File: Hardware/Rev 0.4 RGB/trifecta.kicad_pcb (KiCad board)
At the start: 2 copper layers, 361 x 120.8 mm, 264 parts, among them J1 USB2_C_Receptacle, SW1 SW_Push, SW2 Rotary_Encoder_Switch, SW3 Rotary_Encoder_Switch, SW4 Rotary_Encoder_Switch, U1 ATmega32U4-AU, U2 SRV05-4, Y1 16MHz

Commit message: Changes
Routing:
- net col1: track 99.0 -> 316.3 mm, vias 0 -> 3
- net col2: track 0.00 -> 174.6 mm
- net col3: track 0.00 -> 74.9 mm
- net row1: track 0.45 -> 46.5 mm
- net row0: track 0.26 -> 26.3 mm
- removed copper zone on F.Cu, net GND

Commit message: Update
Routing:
- net col2: track 174.6 -> 235.5 mm, vias 0 -> 2
- net col3: track 74.9 -> 95.1 mm, vias 0 -> 3
- net GND: track 2408.1 -> 2403.4 mm, vias 136 -> 137

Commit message: 03/08-1
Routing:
- net row1: track 46.5 -> 266.6 mm, vias 0 -> 2
- net row0: track 26.3 -> 199.3 mm, vias 0 -> 2
- net row4: track 0.09 -> 148.9 mm, vias 0 -> 4
- net row9: track 0.00 -> 136.2 mm
- net row8: track 0.00 -> 99.6 mm, vias 0 -> 2
- net row6: track 0.61 -> 98.2 mm, vias 0 -> 2
- net row2: track 0.24 -> 88.6 mm, vias 0 -> 2
- net row5: track 0.32 -> 85.9 mm
- net row3: track 2.36 -> 69.7 mm, vias 0 -> 2
- net row7: track 1.46 -> 48.6 mm
- net Net-(LED21-Pad2): track 42.9 -> 50.0 mm
- net +5V: track 1917.1 -> 1920.0 mm, vias 66 -> 67
- net GND: vias 137 -> 136

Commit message: 8/3/2020
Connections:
- U1 pad 10: row6 -> col5
- U1 pad 18: row7 -> col6
- U1 pad 19: row8 -> col4
- U1 pad 29: col6 -> row7
- U1 pad 31: row3 -> row5
- U1 pad 32: col5 -> row6
- U1 pad 37: col4 -> row8
- U1 pad 9: row5 -> row3
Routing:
- net 0col: track 11.0 -> 475.3 mm, vias 0 -> 1
- net col6: track 0.00 -> 355.4 mm, vias 0 -> 2
- net row3: track 69.7 -> 408.9 mm, vias 2 -> 7
- net col5: track 0.00 -> 333.3 mm, vias 0 -> 1
- net row7: track 48.6 -> 377.5 mm
- net row8: track 99.6 -> 412.2 mm, vias 2 -> 5
- net ENC0B: track 0.00 -> 281.1 mm, vias 0 -> 1
- net row9: track 136.2 -> 409.3 mm, vias 0 -> 3
- net ENCB: track 272.8 -> 0.00 mm
- net row2: track 88.6 -> 358.4 mm, vias 2 -> 6
- net row6: track 98.2 -> 354.4 mm, vias 2 -> 4
- net col4: track 0.56 -> 256.4 mm, vias 0 -> 2
- net row5: track 85.9 -> 337.5 mm, vias 0 -> 3
- net ENC2B: track 0.00 -> 224.4 mm, vias 0 -> 2
- net ENC1B: track 0.00 -> 206.8 mm
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
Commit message: Clean up silkscreens, Add ground fill, Generate new gerbers
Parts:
- R1, R6: value 10k -> 10kΩ
- R2, R3: value 5.1k -> 5.1kΩ
- R4, R5: value 22 -> 22Ω
- SW1: value SW_Push -> RESET
- moved SW2 0.22 mm to (323.9, 9.50)
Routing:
- net GND: vias 129 -> 143
- added copper zone on F.Cu, net GND

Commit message: Edit resistor silkscreen, Generate Gerbers
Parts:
- R7: value 510 ohm -> 510Ω
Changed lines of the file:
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@@
     (46 B.CrtYd user)
     (47 F.CrtYd user)
-    (48 B.Fab user)
+    (48 B.Fab user hide)
     (49 F.Fab user hide)
   )
@@
     (tags resistor)
     (attr smd)
-    (fp_text reference R7 (at 0 1.65 270) (layer B.SilkS)
+    (fp_text reference R7 (at 0 1.65 270) (layer B.Fab)
       (effects (font (size 1 1) (thickness 0.15)) (justify mirror))
     )
-    (fp_text value "510 ohm" (at 0 -1.65 270) (layer B.Fab)
+    (fp_text value 510Ω (at 0 1.65104 270) (layer B.SilkS)
       (effects (font (size 1 1) (thickness 0.15)) (justify mirror))
     )

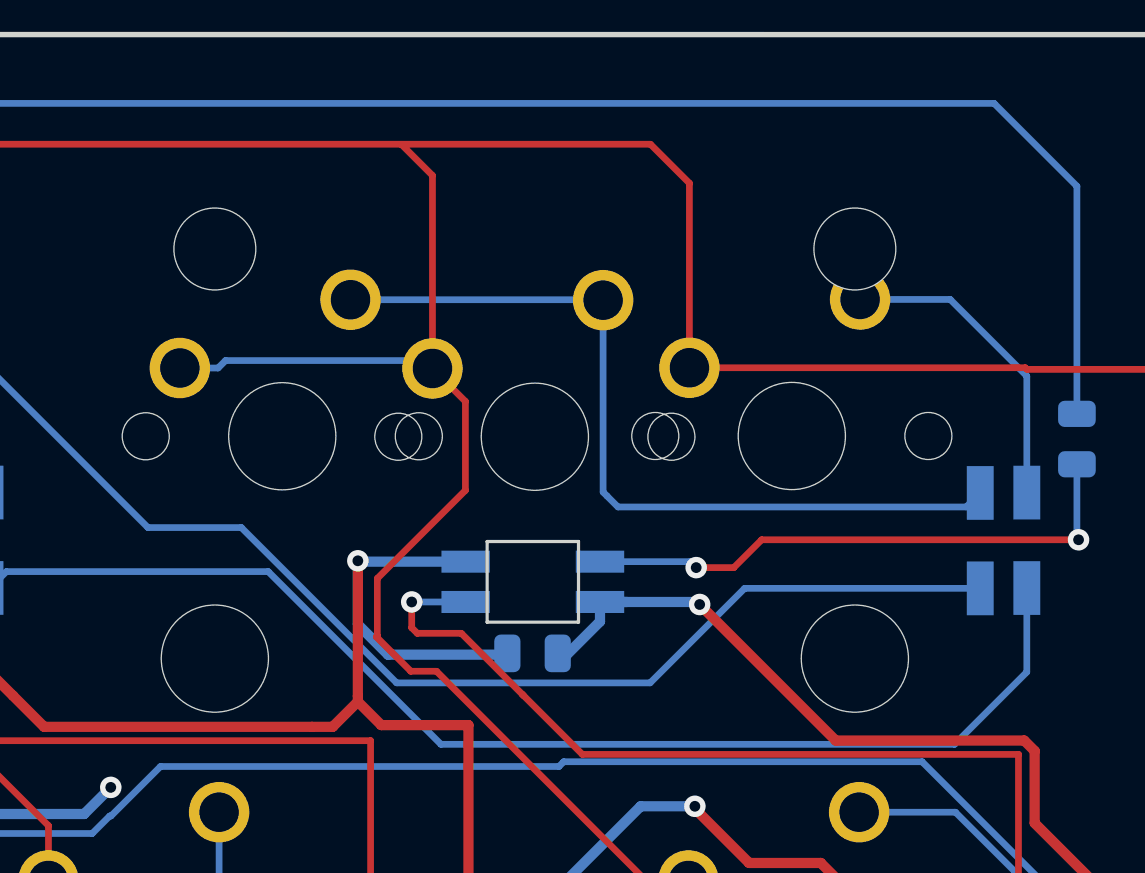
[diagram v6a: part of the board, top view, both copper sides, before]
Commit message: Flip backspace stab regenerate gerbers
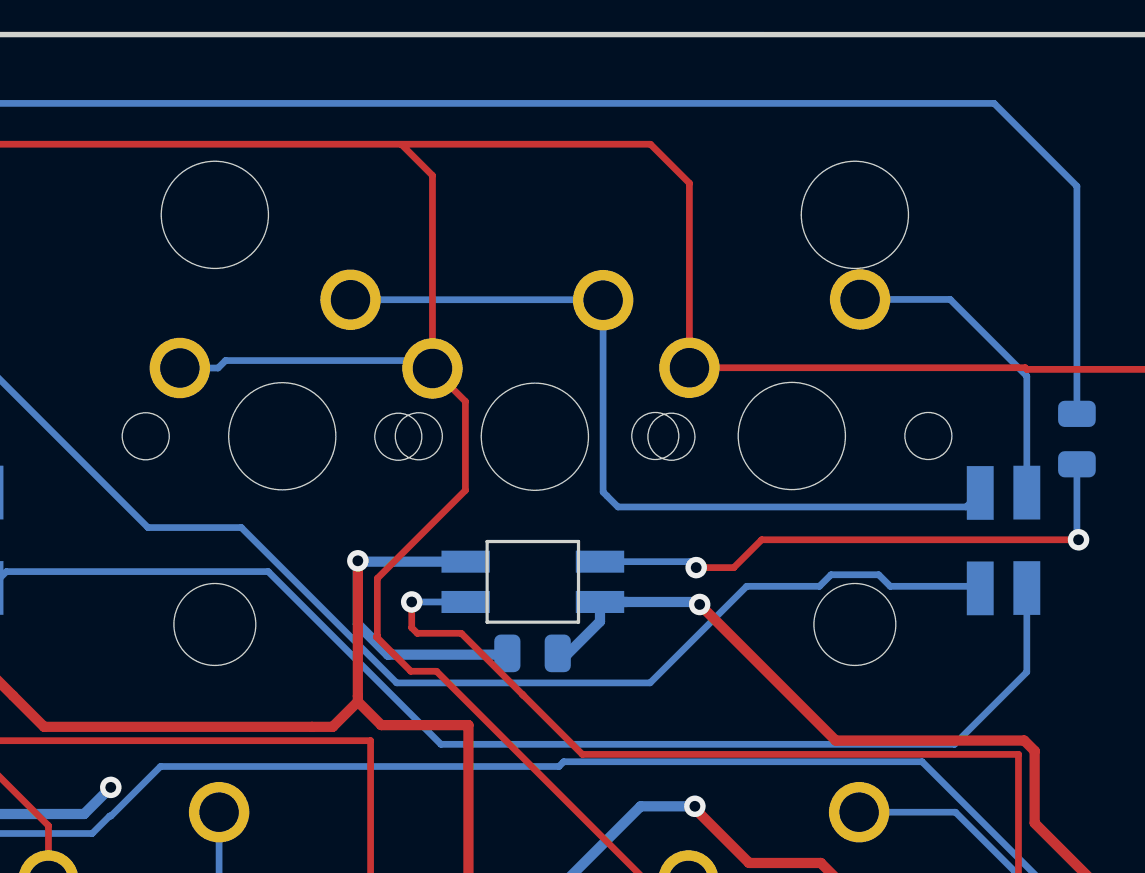
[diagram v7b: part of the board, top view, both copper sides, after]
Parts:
- K_15: footprint MX_Only:MXOnly-2U-NoLED -> MX_Only:MXOnly-2U-ReversedStabilizers-NoLED
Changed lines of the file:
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@@
     (thickness 1.6)
     (drawings 941)
-    (tracks 4299)
+    (tracks 4304)
     (zones 0)
     (modules 264)
@@
     (add_net VBUS)
   )
+  (module MX_Only:MXOnly-2U-ReversedStabilizers-NoLED (layer F.Cu)
+    (at 285.78125 9.434746)
+    (fp_text reference K_15 (at 0 3.175) (layer Dwgs.User)
+      (effects (font (size 1 1) (thickness 0.15)))
+    )
+    (fp_text value KEYSW (at 0 -7.9375) (layer Dwgs.User)
+      (effects (font (size 1 1) (thickness 0.15)))
+    )
+    (fp_line (start 5 -7) (end 7 -7) (layer Dwgs.User) (width 0.15))
+    (fp_line (start 7 -7) (end 7 -5) (layer Dwgs.User) (width 0.15))
+    (fp_line (start 5 7) (end 7 7) (layer Dwgs.User) (width 0.15))
+    (fp_line (start 7 7) (end 7 5) (layer Dwgs.User) (width 0.15))
+    (fp_line (start -7 5) (end -7 7) (layer Dwgs.User) (width 0.15))
+    (fp_line (start -7 7) (end -5 7) (layer Dwgs.User) (width 0.15))
+    (fp_line (start -5 -7) (end -7 -7) (layer Dwgs.User) (width 0.15))
+    (fp_line (start -7 -7) (end -7 -5) (layer Dwgs.User) (width 0.15))
+    (fp_line (start -19.05 -9.525) (end 19.05 -9.525) (layer Dwgs.User) (width 0.15))
+    (fp_line (start 19.05 -9.525) (end 19.05 9.525) (layer Dwgs.User) (width 0.15))
+    (fp_line (start -19.05 9.525) (end 19.05 9.525) (layer Dwgs.User) (width 0.15))
+    (fp_line (start -19.05 9.525) (end -19.05 -9.525) (layer Dwgs.User) (width 0.15))
+    (pad 2 thru_hole circle (at 2.54 -5.08) (size 2.25 2.25) (drill 1.47) (layers *.Cu B.Mask)
+      (net 132 "Net-(D_15-Pad2)"))
+    (pad "" np_thru_hole circle (at 0 0) (size 3.9878 3.9878) (drill 3.9878) (layers *.Cu *.Mask))
+    (pad 1 thru_hole circle (at -3.81 -2.54) (size 2.25 2.25) (drill 1.47) (layers *.Cu B.Mask)
+      (net 95 0col))
+    (pad "" np_thru_hole circle (at -5.08 0 48.0996) (size 1.75 1.75) (drill 1.75) (layers *.Cu *.Mask))
+    (pad "" np_thru_hole circle (at 5.08 0 48.0996) (size 1.75 1.75) (drill 1.75) (layers *.Cu *.Mask))
+    (pad "" np_thru_hole circle (at -11.90625 6.985) (size 3.048 3.048) (drill 3.048) (layers *.Cu *.Mask))
+    (pad "" np_thru_hole circle (at 11.90625 6.985) (size 3.048 3.048) (drill 3.048) (layers *.Cu *.Mask))
+    (pad "" np_thru_hole circle (at -11.90625 -8.255) (size 3.9878 3.9878) (drill 3.9878) (layers *.Cu *.Mask))
+    (pad "" np_thru_hole circle (at 11.90625 -8.255) (size 3.9878 3.9878) (drill 3.9878) (layers *.Cu *.Mask))
+  )
   (module random-keyboard-parts:SKQG-1155865 (layer B.Cu)
     (at 141.29092 78.02574 190)
@@
     (pad "" np_thru_hole circle (at 5.08 0 48.0996) (size 1.75 1.75) (drill 1.75) (layers *.Cu *.Mask))
   )
-  (module MX_Only:MXOnly-2U-NoLED (layer F.Cu)
-    (at 285.78125 9.434746)
-    (fp_text reference K_15 (at 0 3.175) (layer Dwgs.User)
-      (effects (font (size 1 1) (thickness 0.15)))
-    )
-    (fp_text value KEYSW (at 0 -7.9375) (layer Dwgs.User)
-      (effects (font (size 1 1) (thickness 0.15)))
-    )
-    (fp_line (start -19.05 9.525) (end -19.05 -9.525) (layer Dwgs.User) (width 0.15))
-    (fp_line (start -19.05 9.525) (end 19.05 9.525) (layer Dwgs.User) (width 0.15))
-    (fp_line (start 19.05 -9.525) (end 19.05 9.525) (layer Dwgs.User) (width 0.15))
-    (fp_line (start -19.05 -9.525) (end 19.05 -9.525) (layer Dwgs.User) (width 0.15))
-    (fp_line (start -7 -7) (end -7 -5) (layer Dwgs.User) (width 0.15))
-    (fp_line (start -5 -7) (end -7 -7) (layer Dwgs.User) (width 0.15))
-    (fp_line (start -7 7) (end -5 7) (layer Dwgs.User) (width 0.15))
-    (fp_line (start -7 5) (end -7 7) (layer Dwgs.User) (width 0.15))
-    (fp_line (start 7 7) (end 7 5) (layer Dwgs.User) (width 0.15))
-    (fp_line (start 5 7) (end 7 7) (layer Dwgs.User) (width 0.15))
-    (fp_line (start 7 -7) (end 7 -5) (layer Dwgs.User) (width 0.15))
-    (fp_line (start 5 -7) (end 7 -7) (layer Dwgs.User) (width 0.15))
-    (pad 2 thru_hole circle (at 2.54 -5.08) (size 2.25 2.25) (drill 1.47) (layers *.Cu B.Mask)
-      (net 132 "Net-(D_15-Pad2)"))
-    (pad "" np_thru_hole circle (at 0 0) (size 3.9878 3.9878) (drill 3.9878) (layers *.Cu *.Mask))
-    (pad 1 thru_hole circle (at -3.81 -2.54) (size 2.25 2.25) (drill 1.47) (layers *.Cu B.Mask)
-      (net 95 0col))
-    (pad "" np_thru_hole circle (at -5.08 0 48.0996) (size 1.75 1.75) (drill 1.75) (layers *.Cu *.Mask))
-    (pad "" np_thru_hole circle (at 5.08 0 48.0996) (size 1.75 1.75) (drill 1.75) (layers *.Cu *.Mask))
-    (pad "" np_thru_hole circle (at -11.90625 -6.985) (size 3.048 3.048) (drill 3.048) (layers *.Cu *.Mask))
-    (pad "" np_thru_hole circle (at 11.90625 -6.985) (size 3.048 3.048) (drill 3.048) (layers *.Cu *.Mask))
-    (pad "" np_thru_hole circle (at -11.90625 8.255) (size 3.9878 3.9878) (drill 3.9878) (layers *.Cu *.Mask))
-    (pad "" np_thru_hole circle (at 11.90625 8.255) (size 3.9878 3.9878) (drill 3.9878) (layers *.Cu *.Mask))
-  )
   (module MX_Only:MXOnly-1U-NoLED (layer F.Cu)
     (at 276.38336 9.4178)
@@
   (segment (start 148.30298 25.95372) (end 148.30298 19.4183) (width 0.25) (layer B.Cu) (net 7))
   (segment (start 148.30298 19.4183) (end 157.83814 9.88314) (width 0.25) (layer B.Cu) (net 7))
-  (segment (start 293.585822 15.07646) (end 290.069482 18.5928) (width 0.25) (layer B.Cu) (net 7))
-  (segment (start 302.35232 15.07646) (end 293.585822 15.07646) (width 0.25) (layer B.Cu) (net 7))
-  (segment (start 280.63832 18.5928) (end 274.85982 12.8143) (width 0.25) (layer B.Cu) (net 7))
-  (segment (start 290.069482 18.5928) (end 280.63832 18.5928) (width 0.25) (layer B.Cu) (net 7))
-  (segment (start 274.85982 12.8143) (end 271.3863 12.8143) (width 0.25) (layer B.Cu) (net 7))
-  (segment (start 271.3863 12.8143) (end 263.6774 5.1054) (width 0.25) (layer B.Cu) (net 7))
-  (segment (start 263.6774 5.1054) (end 263.6774 4.1529) (width 0.25) (layer B.Cu) (net 7))
-  (segment (start 263.6774 4.1529) (end 261.4295 1.905) (width 0.25) (layer B.Cu) (net 7))
-  (segment (start 261.4295 1.905) (end 254.127 1.905) (width 0.25) (layer B.Cu) (net 7))
-  (segment (start 254.127 1.905) (end 247.9421 8.0899) (width 0.25) (layer B.Cu) (net 7))
-  (segment (start 247.9421 12.60338) (end 246.44184 14.10364) (width 0.25) (layer B.Cu) (net 7))
-  (segment (start 247.9421 8.0899) (end 247.9421 12.60338) (width 0.25) (layer B.Cu) (net 7))
   (segment (start 207.4545 15.88692) (end 206.036406 17.305014) (width 0.25) (layer B.Cu) (net 7))
   (segment (start 210.7946 2.0701) (end 207.4545 5.4102) (width 0.25) (layer B.Cu) (net 7))
@@
   (segment (start 164.35724 7.4422) (end 170.6245 13.70946) (width 0.25) (layer F.Cu) (net 7))
   (segment (start 160.274 7.4422) (end 164.35724 7.4422) (width 0.25) (layer F.Cu) (net 7))
+  (segment (start 247.9421 12.60338) (end 246.44184 14.10364) (width 0.25) (layer B.Cu) (net 7))
+  (segment (start 296.370724 15) (end 293.662282 15) (width 0.25) (layer B.Cu) (net 7))
+  (segment (start 296.799979 14.570745) (end 296.370724 15) (width 0.25) (layer B.Cu) (net 7))
+  (segment (start 298.575021 14.570745) (end 296.799979 14.570745) (width 0.25) (layer B.Cu) (net 7))
+  (segment (start 302.35232 15.07646) (end 302.27586 15) (width 0.25) (layer B.Cu) (net 7))
+  (segment (start 290.069482 18.5928) (end 280.63832 18.5928) (width 0.25) (layer B.Cu) (net 7))
+  (segment (start 254.127 1.905) (end 247.9421 8.0899) (width 0.25) (layer B.Cu) (net 7))
+  (segment (start 293.662282 15) (end 290.069482 18.5928) (width 0.25) (layer B.Cu) (net 7))
+  (segment (start 271.3863 12.8143) (end 263.6774 5.1054) (width 0.25) (layer B.Cu) (net 7))
+  (segment (start 302.27586 15) (end 299.004276 15) (width 0.25) (layer B.Cu) (net 7))
+  (segment (start 280.63832 18.5928) (end 274.85982 12.8143) (width 0.25) (layer B.Cu) (net 7))
+  (segment (start 274.85982 12.8143) (end 271.3863 12.8143) (width 0.25) (layer B.Cu) (net 7))
+  (segment (start 263.6774 5.1054) (end 263.6774 4.1529) (width 0.25) (layer B.Cu) (net 7))
+  (segment (start 263.6774 4.1529) (end 261.4295 1.905) (width 0.25) (layer B.Cu) (net 7))
+  (segment (start 261.4295 1.905) (end 254.127 1.905) (width 0.25) (layer B.Cu) (net 7))
+  (segment (start 299.004276 15) (end 298.575021 14.570745) (width 0.25) (layer B.Cu) (net 7))
+  (segment (start 247.9421 8.0899) (end 247.9421 12.60338) (width 0.25) (layer B.Cu) (net 7))
   (segment (start 58.332481 15.685891) (end 58.332481 16.135433) (width 0.25) (layer B.Cu) (net 8))
   (segment (start 17.99424 15.07138) (end 20.56882 12.4968) (width 0.25) (layer B.Cu) (net 8))
